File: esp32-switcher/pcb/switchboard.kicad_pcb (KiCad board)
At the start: 2 copper layers, 59.5 x 48 mm, 18 parts, among them J1 Conn_01x02, J10 Conn_01x02, J11 Conn_01x02, J12 Conn_01x02, J13 Conn_01x04, J14 Chain Out, J15 Chain In, J2 Conn_01x02, J3 Conn_01x02, J4 Conn_01x02, J5 Conn_01x02, J6 Conn_01x02, J7 Conn_01x02, J8 Conn_01x02, J9 Conn_01x02, U1 HILETGO ESP-32S

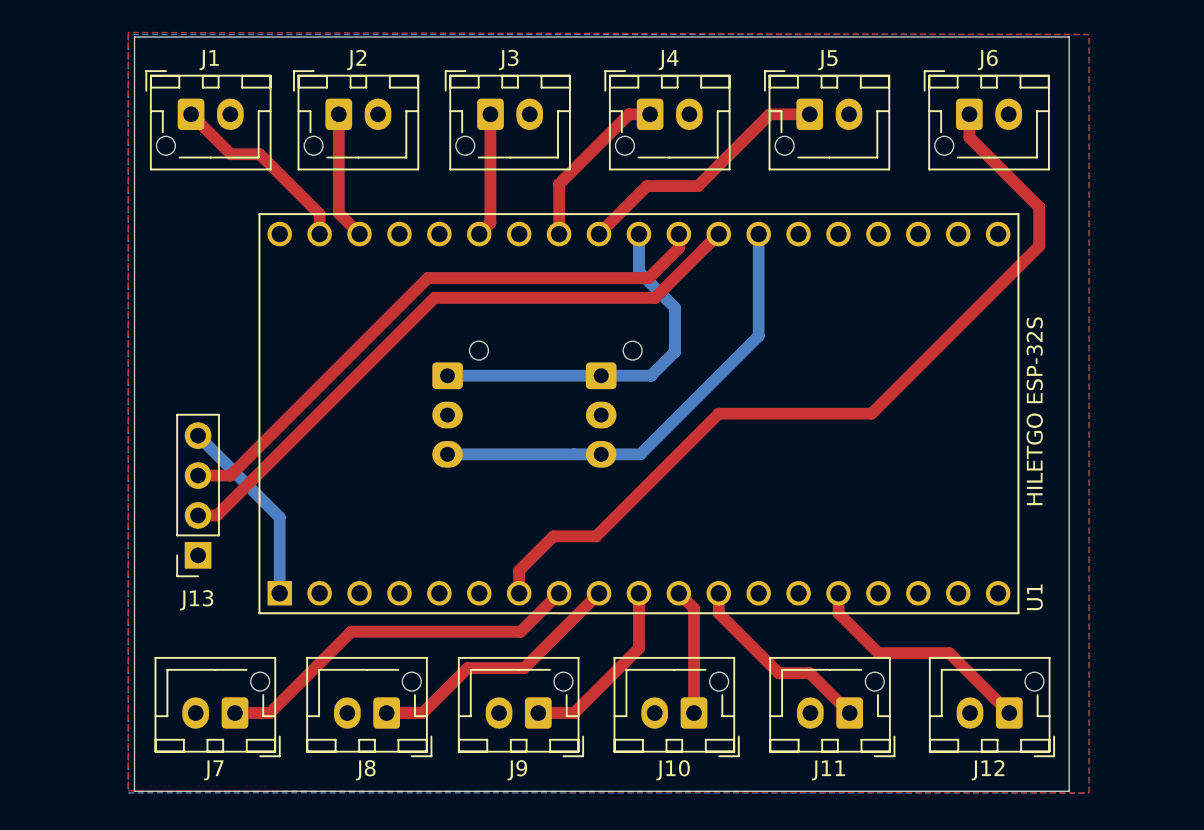
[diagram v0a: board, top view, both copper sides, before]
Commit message: Switchboard v1.2
Switch around all the XA connectors to allow for either top-entry or
side-entry XH connectors.
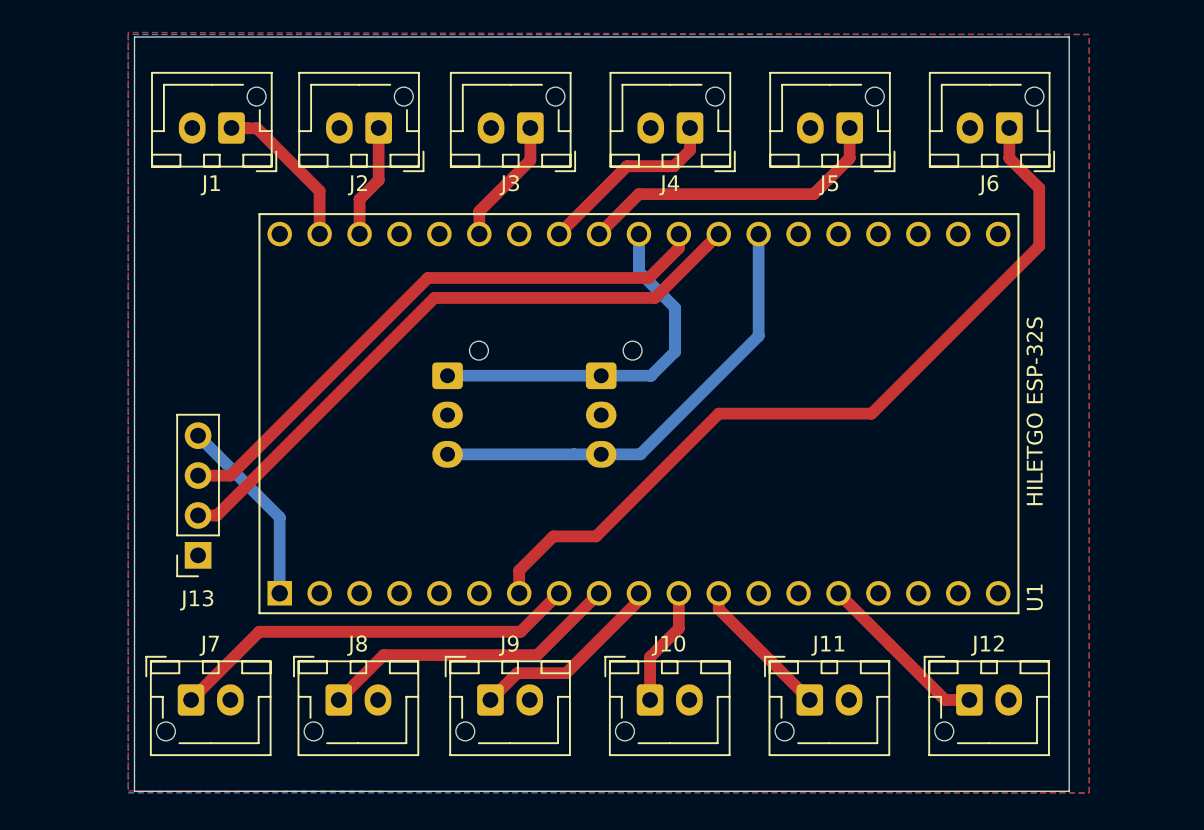
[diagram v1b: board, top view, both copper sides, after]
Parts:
- moved J9 3.16 mm to (144.0, 107.5), turned to 0 degrees
- moved J8 3.16 mm to (134.4, 107.5), turned to 0 degrees
- moved J10 2.91 mm to (154.2, 107.5), turned to 0 degrees
- moved J7 2.91 mm to (125.0, 107.5), turned to 0 degrees
- moved J1 2.71 mm to (127.5, 71.1), turned to 180 degrees
- moved J6 2.68 mm to (177.0, 71.1), turned to 180 degrees
- moved J2 2.68 mm to (136.9, 71.1), turned to 180 degrees
- moved J3 2.68 mm to (146.6, 71.1), turned to 180 degrees
- moved J4 2.68 mm to (156.7, 71.1), turned to 180 degrees
- moved J5 2.68 mm to (166.9, 71.1), turned to 180 degrees
- moved J12 2.67 mm to (174.5, 107.5), turned to 0 degrees
- moved J11 2.67 mm to (164.3, 107.5), turned to 0 degrees
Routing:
- net Net-(J12-Pad1): track 14.8 -> 11.1 mm
- net Net-(J5-Pad1): track 16.6 -> 19.9 mm
- net Net-(J11-Pad1): track 12.2 -> 9.19 mm
- net Net-(J8-Pad1): track 16.7 -> 19.4 mm
- net Net-(J7-Pad1): track 23.8 -> 26.2 mm
- net Net-(J1-Pad1): track 12.1 -> 10.0 mm
- net Net-(J6-Pad1): track 53.3 -> 51.4 mm
- net Net-(J4-Pad1): track 10.8 -> 12.0 mm
- net Net-(J9-Pad1): track 11.6 -> 12.5 mm
- net Net-(J2-Pad1): track 8.17 -> 7.26 mm
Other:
- board text added: "v1.2"
- board text removed: "v1.1"

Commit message: Add mounting holes and 2nd position for serial uart on switchboard
Also, "rescue" components on scart-input board. I gotta figure out what
that's about...
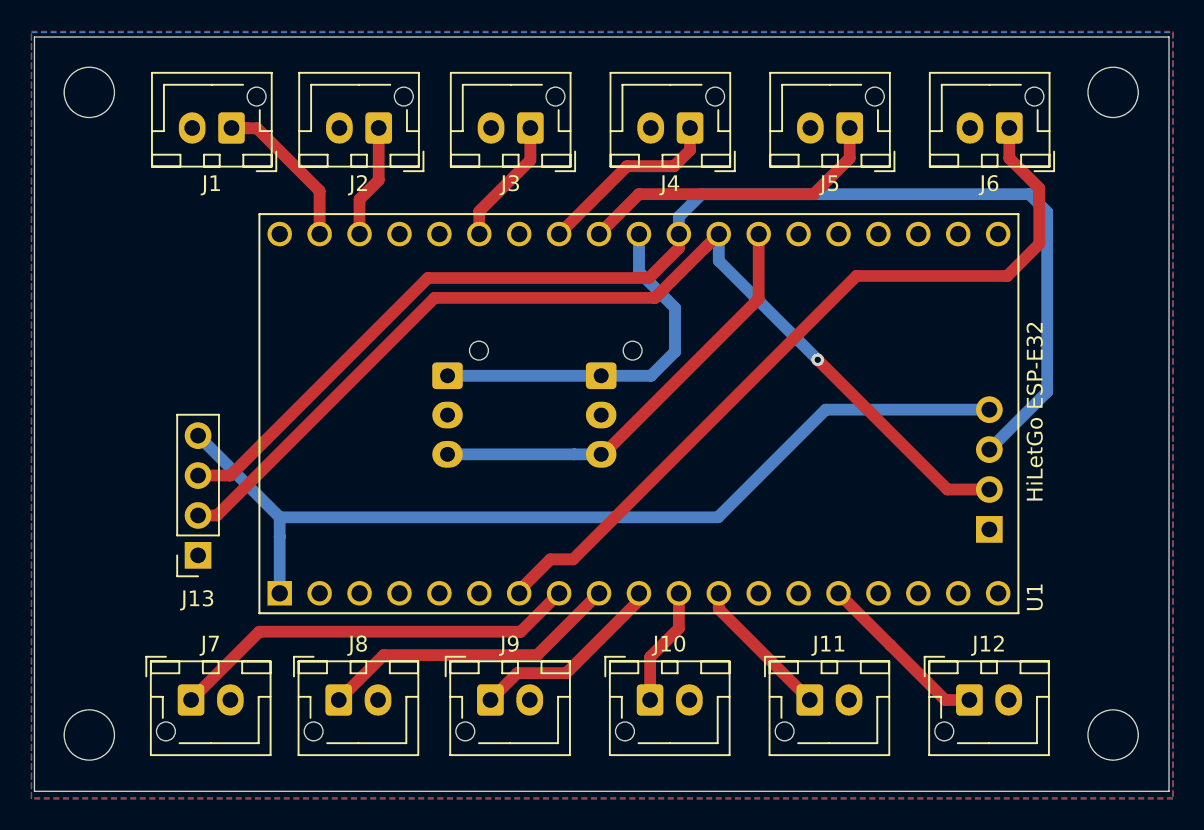
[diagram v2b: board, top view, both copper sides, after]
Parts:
- removed REF**: OSHW-Logo2_9.8x8mm_SilkScreen, Symbol:OSHW-Logo2_9.8x8mm_SilkScreen
- removed REF**: KiCad-Logo2_8mm_SilkScreen, Symbol:KiCad-Logo2_8mm_SilkScreen
- added J16: Conn_01x04, Connector_PinSocket_2.54mm:PinSocket_1x04_P2.54mm_Vertical, B.Cu at (175.8, 96.6)
- added J17: Conn_01x01, MountingHole:MountingHole_3.2mm_M3, F.Cu at (118.5, 68.8)
- added J18: Conn_01x01, MountingHole:MountingHole_3.2mm_M3, F.Cu at (118.5, 109.7)
- added J19: Conn_01x01, MountingHole:MountingHole_3.2mm_M3, F.Cu at (183.6, 68.8)
- added J20: Conn_01x01, MountingHole:MountingHole_3.2mm_M3, F.Cu at (183.6, 109.7)
- U1: value HILETGO ESP-32S -> HiLetGo ESP-E32
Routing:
- net PWR: track 12.2 -> 60.2 mm
- net Net-(J13-Pad3): track 37.5 -> 79.7 mm
- net Net-(J13-Pad2): track 40.6 -> 65.5 mm, vias 0 -> 1
- net Net-(J14-Pad3): track 29.4 -> 28.0 mm
- net Net-(J6-Pad1): track 51.4 -> 50.6 mm
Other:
- board size 59.5 x 48 mm -> 72.2 x 48 mm
- board text added: "v1.3"
- board text removed: "v1.2"
